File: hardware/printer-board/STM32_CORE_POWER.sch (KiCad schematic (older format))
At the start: 9 parts, among them J46 Conn_01x03, U14 AMS1117-3.3

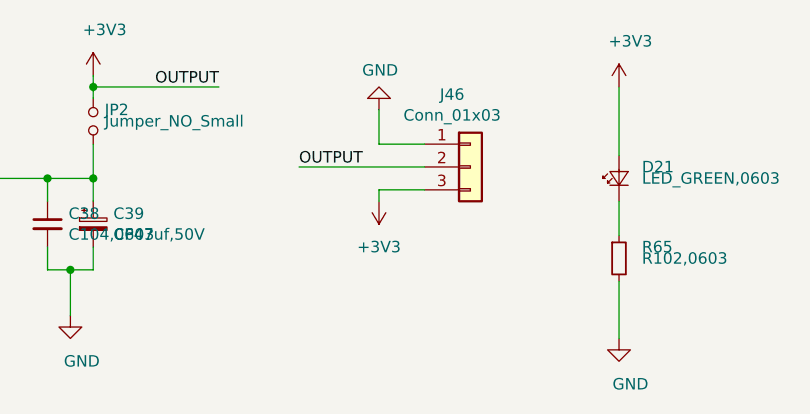
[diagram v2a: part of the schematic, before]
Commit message: update power tree,
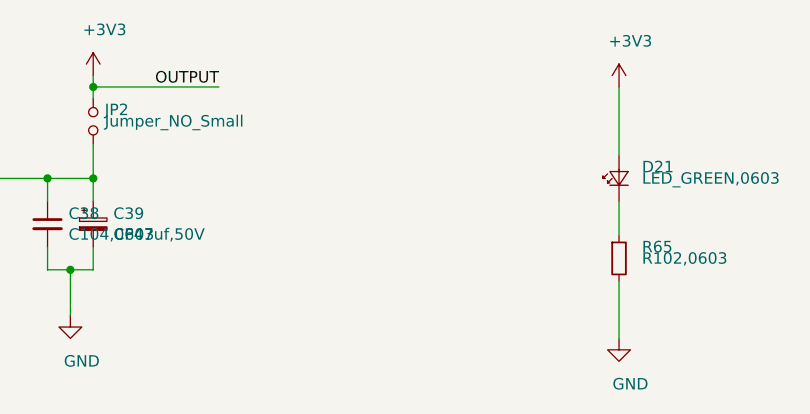
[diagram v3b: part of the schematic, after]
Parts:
- removed J46: Conn_01x03, Connector_PinHeader_2.54mm:PinHeader_1x03_P2.54mm_Vertical, symbol Connector_Generic:Conn_01x03
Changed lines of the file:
@@
 $Descr A4 11693 8268
 encoding utf-8
-Sheet 23 32
+Sheet 21 32
 Title ""
 Date ""
@@
 	1    0    0    -1
 $EndComp
-$Comp
-L Connector_Generic:Conn_01x03 J?
-U 1 1 5C078669
-P 4450 1300
-AR Path="/5C0BBB2B/5C078669" Ref="J?"  Part="1"
-AR Path="/5C0BFA48/5C078669" Ref="J?"  Part="1"
-AR Path="/5CC29851/5CC2B423/5C078669" Ref="J46"  Part="1"
-AR Path="/5C078669" Ref="J46"  Part="1"
-F 0 "J46" H 4370 1617 50  0000 C CNN
-F 1 "Conn_01x03" H 4370 1526 50  0000 C CNN
-F 2 "Connector_PinHeader_2.54mm:PinHeader_1x03_P2.54mm_Vertical" H 4450 1300 50  0001 C CNN
-F 3 "~" H 4450 1300 50  0001 C CNN
-	1    4450 1300
-	1    0    0    -1
-$EndComp
-$Comp
-L power:GND #PWR?
-U 1 1 5C07899D
-P 4050 1050
-AR Path="/5C0BBB2B/5C07899D" Ref="#PWR?"  Part="1"
-AR Path="/5C0BFA48/5C07899D" Ref="#PWR?"  Part="1"
-AR Path="/5CC29851/5CC2B423/5C07899D" Ref="#PWR06"  Part="1"
-AR Path="/5C07899D" Ref="#PWR06"  Part="1"
-F 0 "#PWR06" H 4050 800 50  0001 C CNN
-F 1 "GND" H 4055 877 50  0000 C CNN
-F 2 "" H 4050 1050 50  0001 C CNN
-F 3 "" H 4050 1050 50  0001 C CNN
-	1    4050 1050
-	1    0    0    1
-$EndComp
-Wire Wire Line
-	4250 1200 4050 1200
-Wire Wire Line
-	4050 1200 4050 1050
-Wire Wire Line
-	4250 1400 4050 1400
-Wire Wire Line
-	4050 1400 4050 1450
 Text Label 3350 950  2    50   ~ 0
 OUTPUT
 Wire Wire Line
 	2800 950  3350 950
-Text Label 3700 1300 0    50   ~ 0
-OUTPUT
-Wire Wire Line
-	4250 1300 3700 1300
-$Comp
-L power:+3V3 #PWR05
-U 1 1 5C0C0902
-P 2800 900
-F 0 "#PWR05" H 2800 750 50  0001 C CNN
-F 1 "+3V3" H 2850 1100 50  0000 C CNN
-F 2 "" H 2800 900 50  0001 C CNN
-F 3 "" H 2800 900 50  0001 C CNN
-	1    2800 900
-	1    0    0    -1
-$EndComp
-$Comp
-L power:+3V3 #PWR07
-U 1 1 5C0C0B31
-P 4050 1450
-F 0 "#PWR07" H 4050 1300 50  0001 C CNN
-F 1 "+3V3" H 4050 1650 50  0000 C CNN
-F 2 "" H 4050 1450 50  0001 C CNN
-F 3 "" H 4050 1450 50  0001 C CNN
-	1    4050 1450
-	1    0    0    1
-$EndComp
 $Comp
 L taobao-r:R102,0603 R?
@@
 	5100 1800 5100 2050
 $Comp
-L power:+3V3 #PWR08
-U 1 1 5C0C1334
-P 5100 950
-F 0 "#PWR08" H 5100 800 50  0001 C CNN
-F 1 "+3V3" H 5150 1150 50  0000 C CNN
-F 2 "" H 5100 950 50  0001 C CNN
-F 3 "" H 5100 950 50  0001 C CNN
-	1    5100 950
-	1    0    0    -1
-$EndComp
-$Comp
 L taobao-led:LED_GREEN,0603 D21
 U 1 1 5C0D46AA
@@
 	1    0    0    -1
 $EndComp
+$Comp
+L power:+3V3 #PWR?
+U 1 1 5CC75A45
+P 2800 900
+F 0 "#PWR?" H 2800 750 50  0001 C CNN
+F 1 "+3V3" H 2850 1100 50  0000 C CNN
+F 2 "" H 2800 900 50  0001 C CNN
+F 3 "" H 2800 900 50  0001 C CNN
+	1    2800 900
+	1    0    0    -1
+$EndComp
+$Comp
+L power:+3V3 #PWR?
+U 1 1 5CC75A67
+P 5100 950
+F 0 "#PWR?" H 5100 800 50  0001 C CNN
+F 1 "+3V3" H 5150 1150 50  0000 C CNN
+F 2 "" H 5100 950 50  0001 C CNN
+F 3 "" H 5100 950 50  0001 C CNN
+	1    5100 950
+	1    0    0    -1
+$EndComp

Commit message: update,
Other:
- moved on the sheet: C37, C38, C39, D21, JP1, JP2, R65, U14

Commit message: update,
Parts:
- D21: value LED_GREEN,0603 -> 3v3 HEALTHY
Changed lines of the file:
@@
 $Descr A4 11693 8268
 encoding utf-8
-Sheet 19 32
+Sheet 18 32
 Title ""
 Date ""
@@
 P 6200 3750
 F 0 "D21" V 6250 3650 50  0000 R CNN
-F 1 "LED_GREEN,0603" V 6200 3650 50  0000 R CNN
+F 1 "3v3 HEALTHY" V 6200 3650 50  0000 R CNN
 F 2 "LED_SMD:LED_0603_1608Metric_Pad1.05x0.95mm_HandSolder" V 6200 3750 50  0001 C CNN
 F 3 "" V 6200 3750 50  0001 C CNN

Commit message: update,
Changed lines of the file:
@@
 $Descr A4 11693 8268
 encoding utf-8
-Sheet 18 33
+Sheet 17 34
 Title ""
 Date ""
@@
 AR Path="/5CC29851/5CC2B423/5C0AD747" Ref="U14"  Part="1"
 AR Path="/5C0AD747" Ref="U14"  Part="1"
-F 0 "U14" H 4500 4000 50  0000 C CNN
+AR Path="/5CC29851/5CC86673/5C0AD747" Ref="U?"  Part="1"
+F 0 "U?" H 4500 4000 50  0000 C CNN
 F 1 "AMS1117-3.3" H 4500 3900 50  0000 C CNN
 F 2 "Package_TO_SOT_SMD:SOT-223-3_TabPin2" H 4500 3900 50  0001 C CNN
@@
 AR Path="/5CC29851/5CC2B423/5C0AD74D" Ref="C37"  Part="1"
 AR Path="/5C0AD74D" Ref="C37"  Part="1"
-F 0 "C37" H 3709 3946 50  0000 R CNN
+AR Path="/5CC29851/5CC86673/5C0AD74D" Ref="C?"  Part="1"
+F 0 "C?" H 3709 3946 50  0000 R CNN
 F 1 "C104,0603" H 3709 3855 50  0000 R CNN
 F 2 "Capacitor_SMD:C_0603_1608Metric_Pad1.05x0.95mm_HandSolder" H 3800 3900 50  0001 C CNN
@@
 AR Path="/5CC29851/5CC2B423/5C0D4463" Ref="#PWR03"  Part="1"
 AR Path="/5C0D4463" Ref="#PWR03"  Part="1"
-F 0 "#PWR03" H 4500 4050 50  0001 C CNN
+AR Path="/5CC29851/5CC86673/5C0D4463" Ref="#PWR?"  Part="1"
+F 0 "#PWR?" H 4500 4050 50  0001 C CNN
 F 1 "GND" H 4550 4100 50  0000 C CNN
 F 2 "" H 4500 4300 50  0001 C CNN
@@
 AR Path="/5CC29851/5CC2B423/5C0D4465" Ref="C38"  Part="1"
 AR Path="/5C0D4465" Ref="C38"  Part="1"
-F 0 "C38" H 5150 3950 50  0000 L CNN
+AR Path="/5CC29851/5CC86673/5C0D4465" Ref="C?"  Part="1"
+F 0 "C?" H 5150 3950 50  0000 L CNN
 F 1 "C104,0603" H 5150 3900 50  0000 L CNN
 F 2 "Capacitor_SMD:C_0603_1608Metric_Pad1.05x0.95mm_HandSolder" H 5050 3900 50  0001 C CNN
@@
 AR Path="/5CC29851/5CC2B423/5C04F461" Ref="C39"  Part="1"
 AR Path="/5C04F461" Ref="C39"  Part="1"
-F 0 "C39" H 5350 3950 50  0000 L CNN
+AR Path="/5CC29851/5CC86673/5C04F461" Ref="C?"  Part="1"
+F 0 "C?" H 5350 3950 50  0000 L CNN
 F 1 "CP47uf,50V" H 5350 3900 50  0000 L CNN
 F 2 "w_smd_cap:c_elec_6.3x7.7" H 5250 3900 50  0001 C CNN
@@
 AR Path="/5CC29851/5CC2B423/5C0C1058" Ref="R65"  Part="1"
 AR Path="/5C0C1058" Ref="R65"  Part="1"
-F 0 "R65" H 6300 4150 50  0000 L CNN
+AR Path="/5CC29851/5CC86673/5C0C1058" Ref="R?"  Part="1"
+F 0 "R?" H 6300 4150 50  0000 L CNN
 F 1 "R102,0603" H 6300 4100 50  0000 L CNN
 F 2 "Resistor_SMD:R_0603_1608Metric_Pad1.05x0.95mm_HandSolder" H 6200 4100 50  0001 C CNN
@@
 AR Path="/5CC29851/5CC2B423/5C0C105F" Ref="#PWR09"  Part="1"
 AR Path="/5C0C105F" Ref="#PWR09"  Part="1"
-F 0 "#PWR09" H 6200 4200 50  0001 C CNN
+AR Path="/5CC29851/5CC86673/5C0C105F" Ref="#PWR?"  Part="1"
+F 0 "#PWR?" H 6200 4200 50  0001 C CNN
 F 1 "GND" H 6250 4250 50  0000 C CNN
 F 2 "" H 6200 4450 50  0001 C CNN
@@
 U 1 1 5C0D46AA
 P 6200 3750
-F 0 "D21" V 6250 3650 50  0000 R CNN
+AR Path="/5CC29851/5CC2B423/5C0D46AA" Ref="D21"  Part="1"
+AR Path="/5CC29851/5CC86673/5C0D46AA" Ref="D?"  Part="1"
+F 0 "D?" V 6250 3650 50  0000 R CNN
 F 1 "3v3 HEALTHY" V 6200 3650 50  0000 R CNN
 F 2 "LED_SMD:LED_0603_1608Metric_Pad1.05x0.95mm_HandSolder" V 6200 3750 50  0001 C CNN
@@
 U 1 1 5C148323
 P 3800 3450
-F 0 "JP1" V 3750 3500 50  0000 L CNN
+AR Path="/5CC29851/5CC2B423/5C148323" Ref="JP1"  Part="1"
+AR Path="/5CC29851/5CC86673/5C148323" Ref="JP?"  Part="1"
+F 0 "JP?" V 3750 3500 50  0000 L CNN
 F 1 "Jumper_NO_Small" V 3800 3500 50  0000 L CNN
 F 2 "Jumper:SolderJumper-2_P1.3mm_Bridged2Bar_RoundedPad1.0x1.5mm" H 3800 3450 50  0001 C CNN
@@
 U 1 1 5C148F3B
 P 5250 3450
-F 0 "JP2" V 5200 3500 50  0000 L CNN
+AR Path="/5CC29851/5CC2B423/5C148F3B" Ref="JP2"  Part="1"
+AR Path="/5CC29851/5CC86673/5C148F3B" Ref="JP?"  Part="1"
+F 0 "JP?" V 5200 3500 50  0000 L CNN
 F 1 "Jumper_NO_Small" V 5250 3500 50  0000 L CNN
 F 2 "Jumper:SolderJumper-2_P1.3mm_Bridged2Bar_RoundedPad1.0x1.5mm" H 5250 3450 50  0001 C CNN
@@
 AR Path="/5CC29851/5CC2B423/5C14BD92" Ref="#PWR04"  Part="1"
 AR Path="/5C14BD92" Ref="#PWR04"  Part="1"
-F 0 "#PWR04" H 5150 4050 50  0001 C CNN
+AR Path="/5CC29851/5CC86673/5C14BD92" Ref="#PWR?"  Part="1"
+F 0 "#PWR?" H 5150 4050 50  0001 C CNN
 F 1 "GND" H 5200 4100 50  0000 C CNN
 F 2 "" H 5150 4300 50  0001 C CNN
@@
 AR Path="/5CC29851/5CC2B423/5C14C0B1" Ref="#PWR02"  Part="1"
 AR Path="/5C14C0B1" Ref="#PWR02"  Part="1"
-F 0 "#PWR02" H 3800 4050 50  0001 C CNN
+AR Path="/5CC29851/5CC86673/5C14C0B1" Ref="#PWR?"  Part="1"
+F 0 "#PWR?" H 3800 4050 50  0001 C CNN
 F 1 "GND" H 3850 4100 50  0000 C CNN
 F 2 "" H 3800 4300 50  0001 C CNN
@@
 U 1 1 5C153651
 P 3800 3300
-F 0 "#PWR01" H 3800 3150 50  0001 C CNN
+AR Path="/5CC29851/5CC2B423/5C153651" Ref="#PWR01"  Part="1"
+AR Path="/5CC29851/5CC86673/5C153651" Ref="#PWR?"  Part="1"
+F 0 "#PWR?" H 3800 3150 50  0001 C CNN
 F 1 "+5V" H 3850 3500 50  0000 C CNN
 F 2 "" H 3800 3300 50  0001 C CNN
@@
 U 1 1 5CC75A45
 P 5250 3250
-F 0 "#PWR081" H 5250 3100 50  0001 C CNN
+AR Path="/5CC29851/5CC2B423/5CC75A45" Ref="#PWR081"  Part="1"
+AR Path="/5CC29851/5CC86673/5CC75A45" Ref="#PWR?"  Part="1"
+F 0 "#PWR?" H 5250 3100 50  0001 C CNN
 F 1 "+3V3" H 5300 3450 50  0000 C CNN
 F 2 "" H 5250 3250 50  0001 C CNN
@@
 U 1 1 5CC75A67
 P 6200 3350
-F 0 "#PWR082" H 6200 3200 50  0001 C CNN
+AR Path="/5CC29851/5CC2B423/5CC75A67" Ref="#PWR082"  Part="1"
+AR Path="/5CC29851/5CC86673/5CC75A67" Ref="#PWR?"  Part="1"
+F 0 "#PWR?" H 6200 3200 50  0001 C CNN
 F 1 "+3V3" H 6250 3550 50  0000 C CNN
 F 2 "" H 6200 3350 50  0001 C CNN
